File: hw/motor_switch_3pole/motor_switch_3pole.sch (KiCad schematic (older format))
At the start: 22 parts, among them J1 WAGO 2081-1123, J2 WAGO 233-506, Q1 BSS138, Q2 BSS138

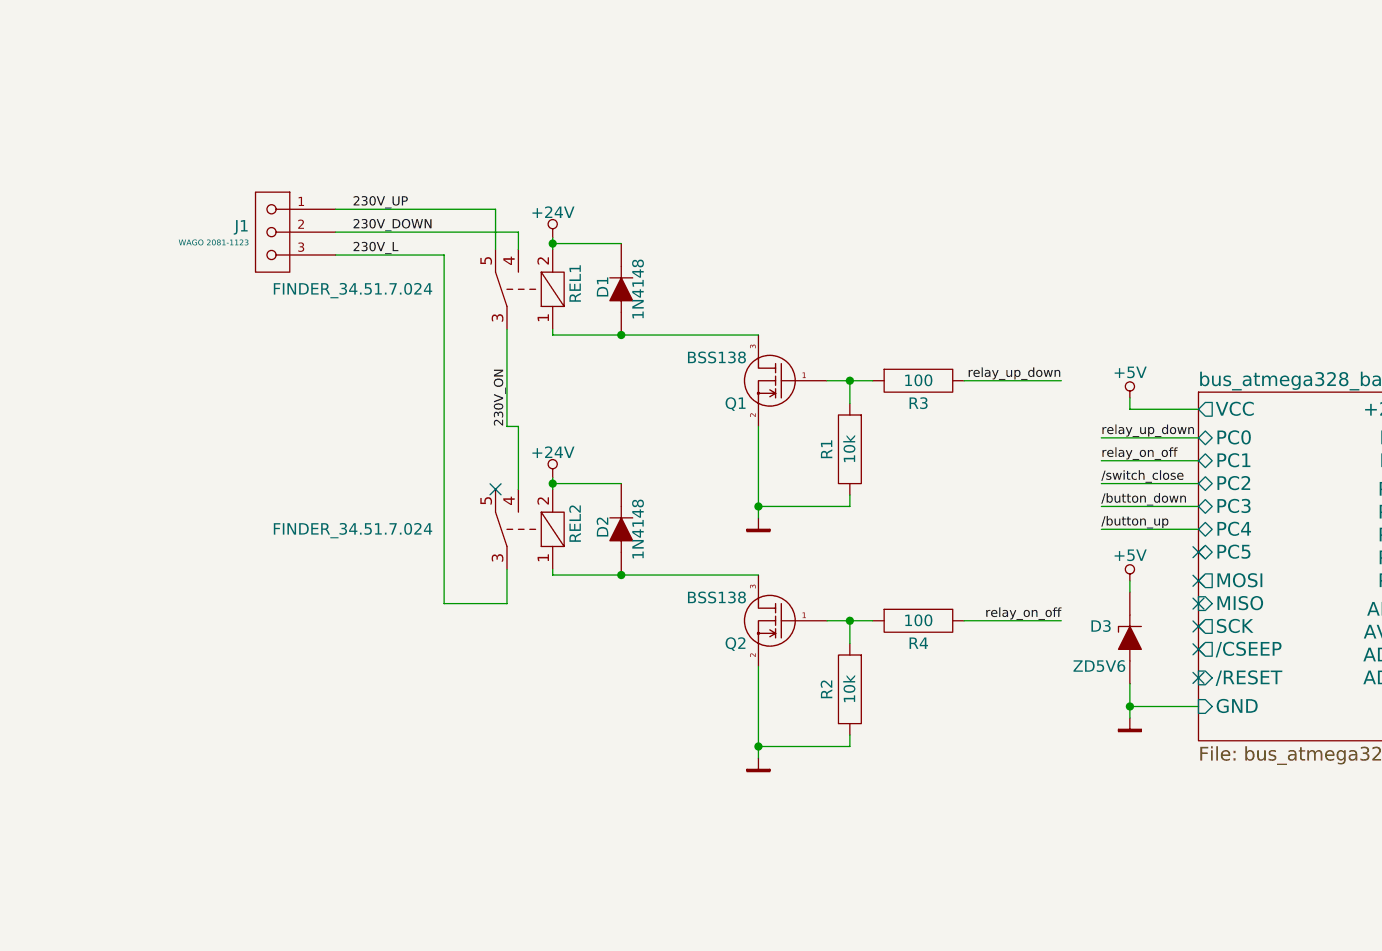
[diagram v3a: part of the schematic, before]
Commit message: Fixed relay pinout bug
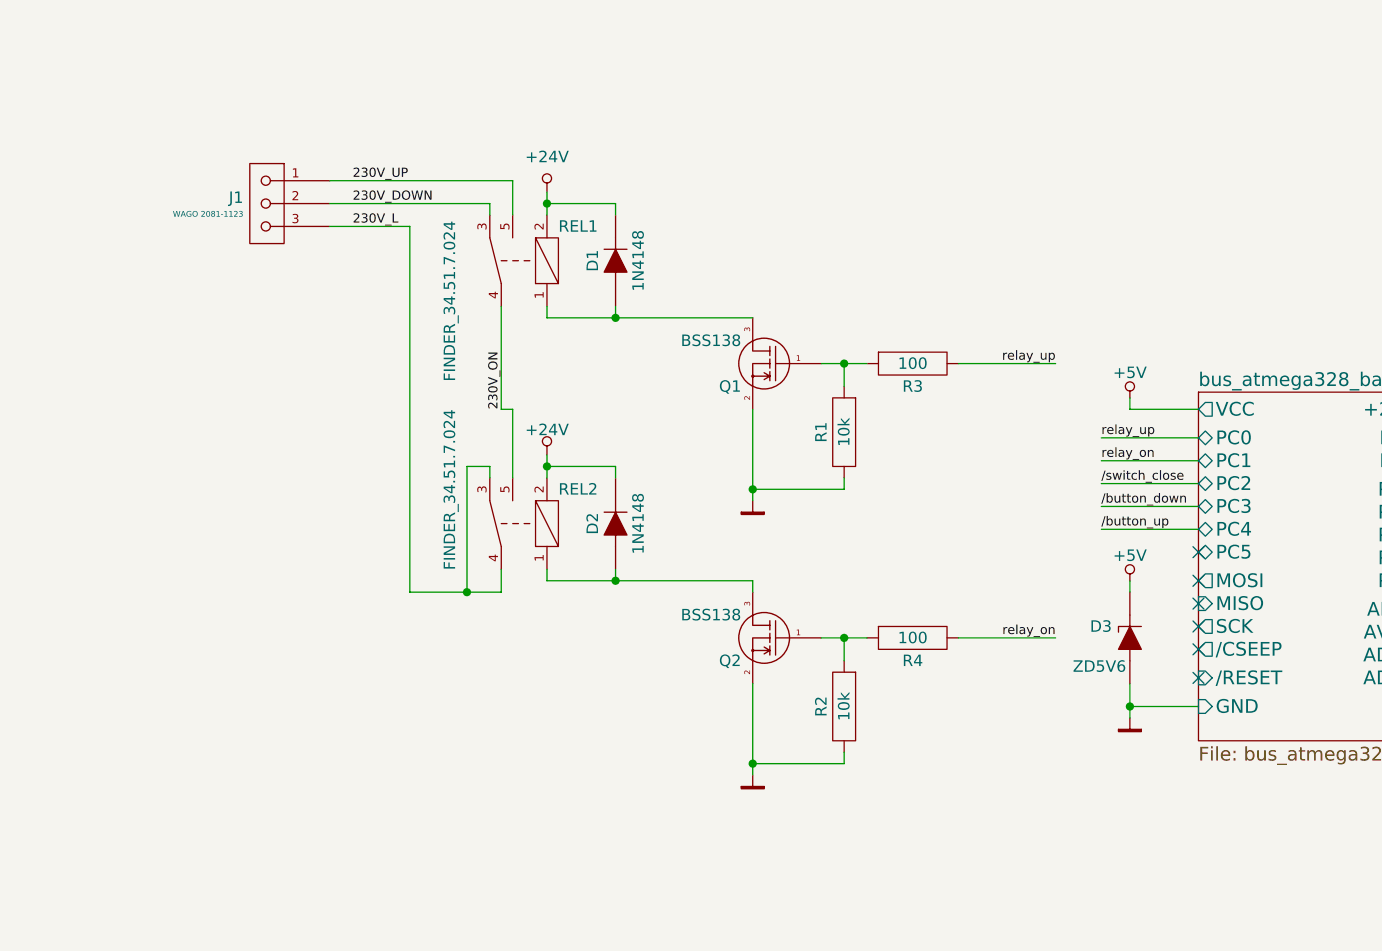
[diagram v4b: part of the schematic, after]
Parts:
- removed REL1, REL2: FINDER_34.51.7.024, Relay:finder_34.51_1xUM, symbol FINDER_36.11-4001
- added REL1, REL2: FINDER_34.51.7.024, Relay:finder_34.51_1xUM, symbol FINDER_34.51.7.024
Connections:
- net +24V: now also REL1.2 (-), REL2.2 (-)
- net 230V_DOWN: now also REL1.3
- net 230V_L: now also REL2.3, REL2.4
- net 230V_ON: now also REL1.4, REL2.5
- net 230V_UP: now also REL1.5
- net at D1.1 (A), Q1.3 (D): now also REL1.1 (+)
- net at D2.1 (A), Q2.3 (D): now also REL2.1 (+)
- net relay_on_off renamed relay_on
- net relay_up_down renamed relay_up
- no-connect marks 20 -> 19
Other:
- moved on the sheet: D1, D2, J1, Q1, Q2, R1, R2, R3, R4
